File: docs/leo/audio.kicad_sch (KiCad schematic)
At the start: 9 parts, among them IC14 74LS08, IC24 74LS74, IC32 GA20, IC45 74LS139, IC47 74LS32, IC48 74LS374, IC49 74LS374, IC8 74LS86

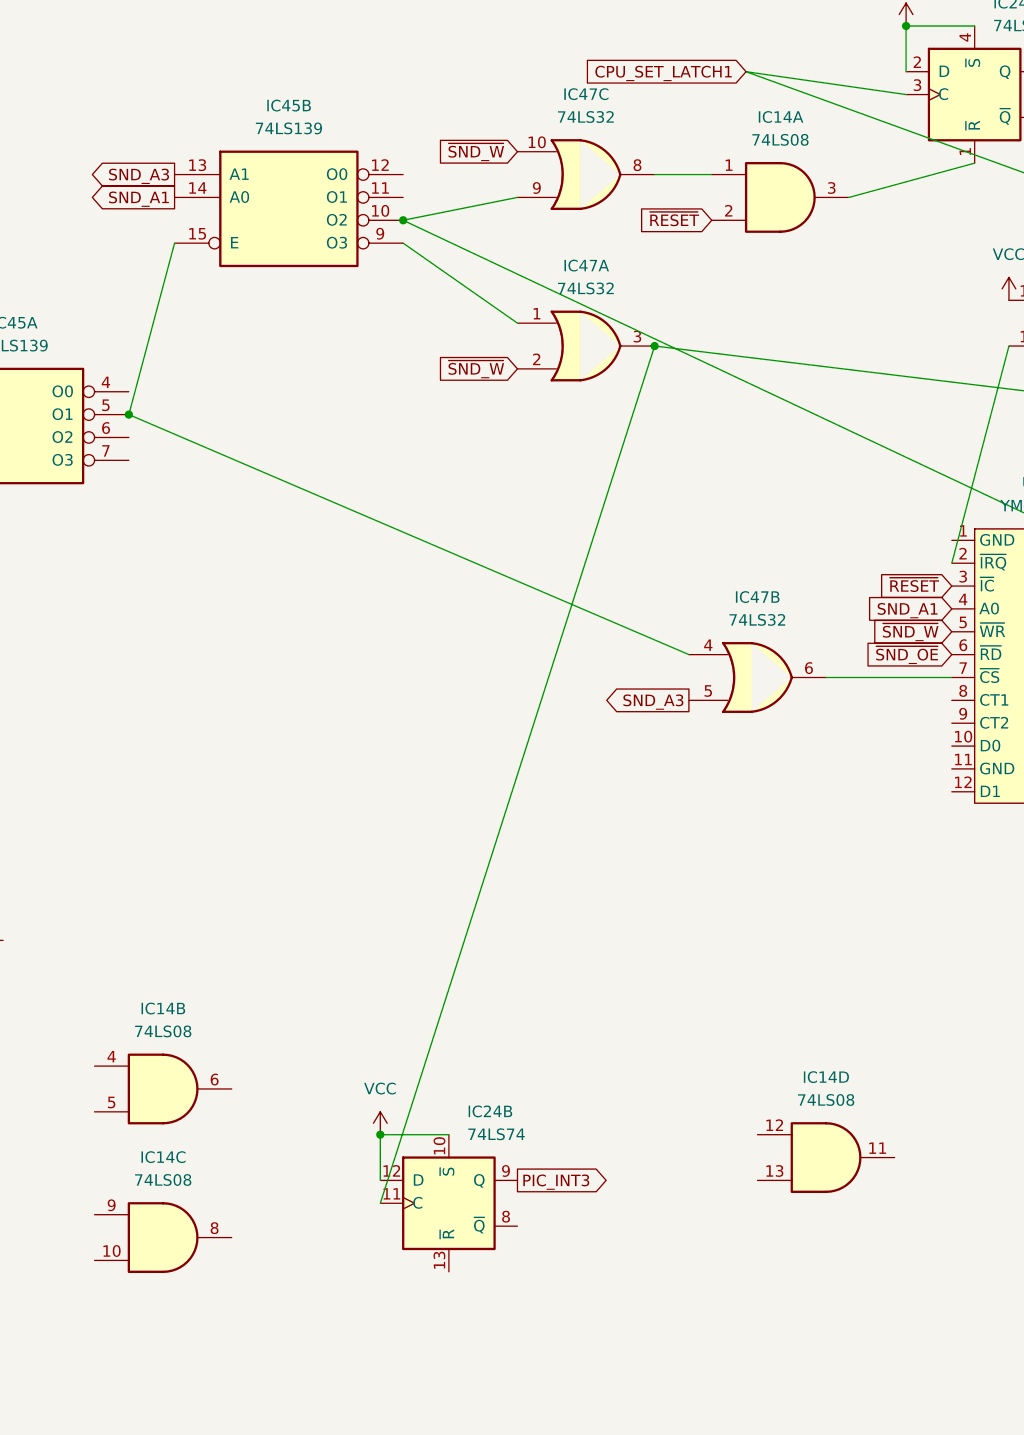
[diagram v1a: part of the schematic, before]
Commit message: Add ym filters and misinx path Upgrade to kicad 7
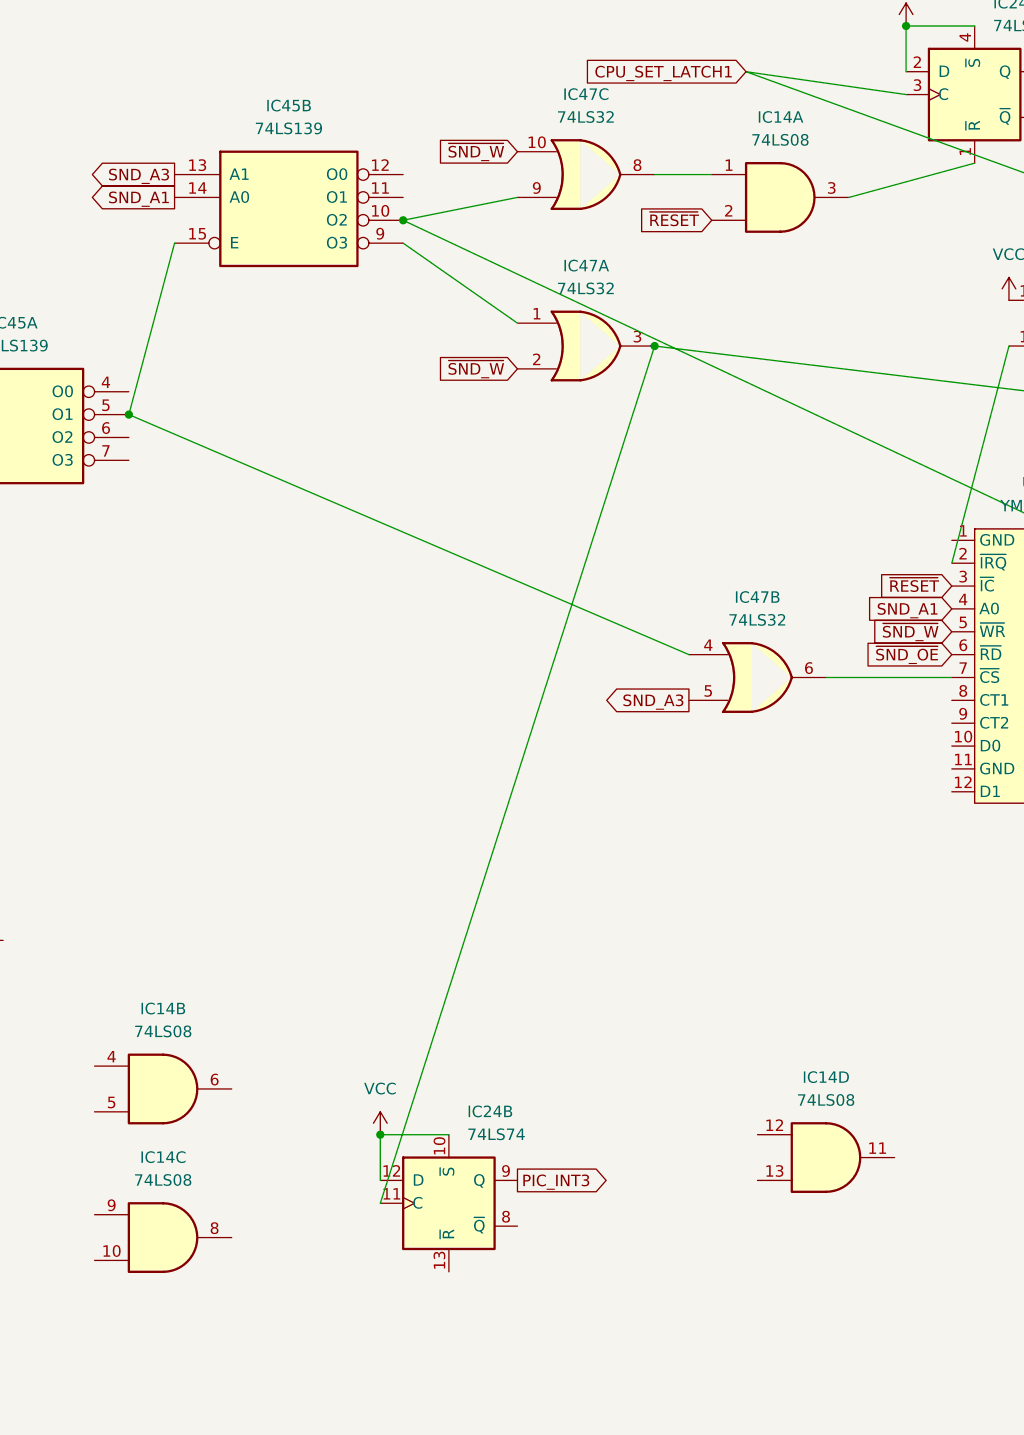
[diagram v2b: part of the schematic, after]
